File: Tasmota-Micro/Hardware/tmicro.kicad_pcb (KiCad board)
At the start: 4 copper layers, 33.5 x 13 mm, 16 parts, among them P2 CONN_01X02, P3 CONN_01X02, P4 CONN_01X04, P5 CONN_01X02, P6 CONN_01X02, P7 USB_A, Q1 IRLML6244, Q2 IRLML6244, U1 MCP1703, U2 ESP-01v090

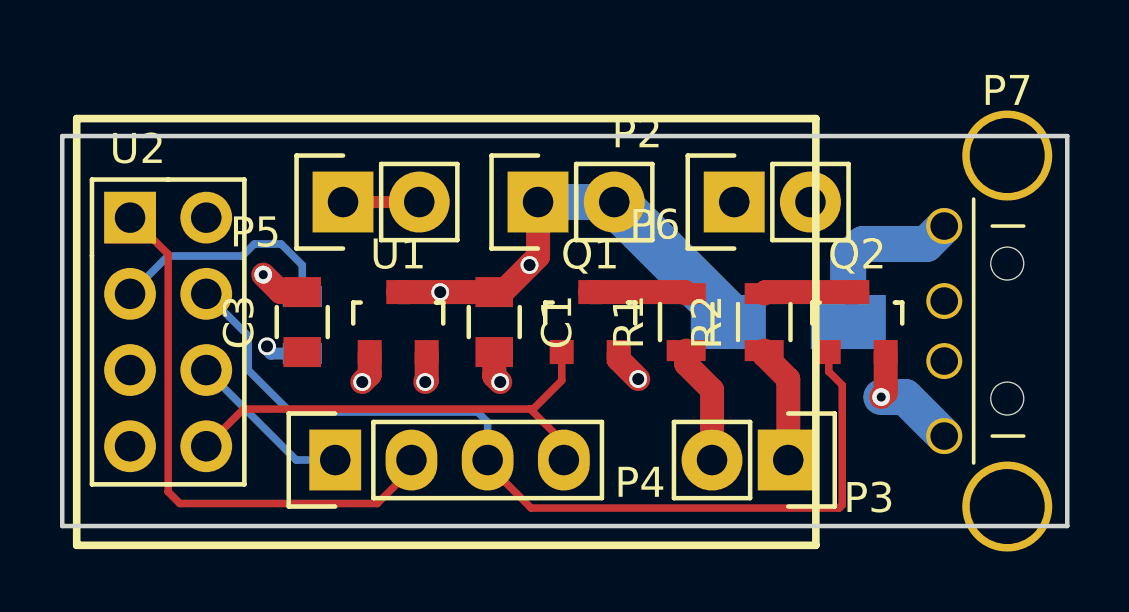
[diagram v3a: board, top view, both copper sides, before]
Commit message: merge back to master as 2 layers
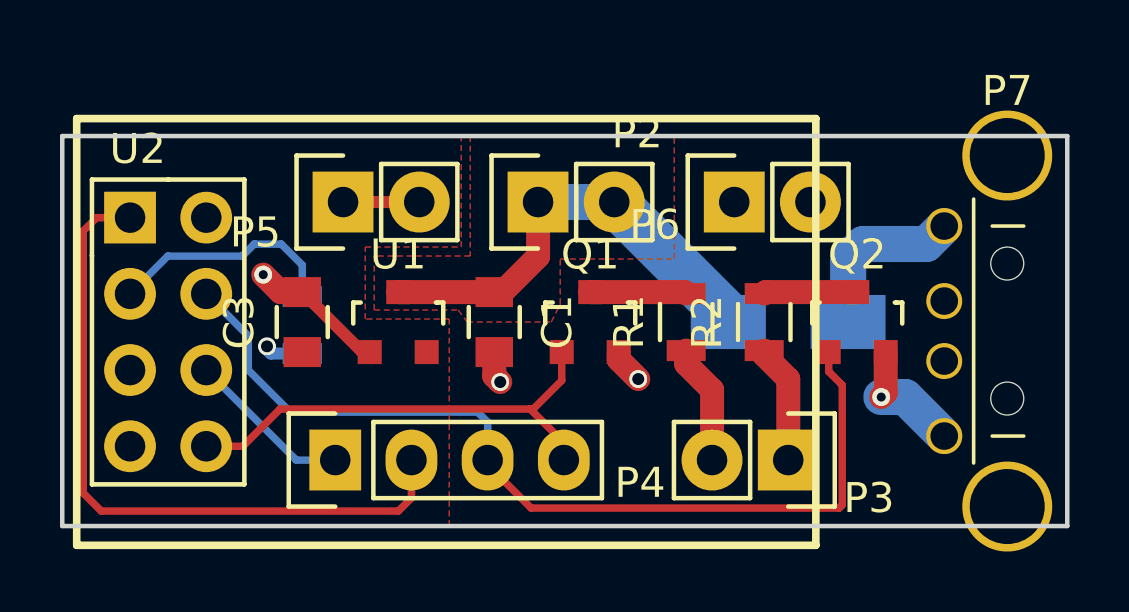
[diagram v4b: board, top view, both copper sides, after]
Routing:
- net TX: track 19.8 -> 23.1 mm
- net GND: track 9.39 -> 11.4 mm, vias 5 -> 4
- net +3V3: track 5.75 -> 4.73 mm, vias 2 -> 1
- net VPP: vias 2 -> 0
- added copper zone on F.Cu, net +3V3
- added copper zone on B.Cu, net GND
- added copper zone on F.Cu, net VPP
- removed copper zone on In1.Cu, net +3V3
- removed copper zone on In2.Cu, net GND
- removed copper zone on In1.Cu, net VPP
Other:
- copper layers 4 -> 2
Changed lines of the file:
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@@
   (general
     (links 31)
-    (no_connects 1)
+    (no_connects 0)
     (area 144.407 102.575 201.425001 126.875)
     (thickness 1.6)
     (drawings 14)
-    (tracks 107)
+    (tracks 97)
     (zones 0)
     (modules 16)
@@
   (layers
     (0 F.Cu signal)
-    (1 In1.Cu signal)
-    (2 In2.Cu signal)
     (31 B.Cu signal)
     (32 B.Adhes user)
@@
     (34 B.Paste user)
     (35 F.Paste user)
-    (36 B.SilkS user)
-    (37 F.SilkS user)
+    (36 B.SilkS user hide)
+    (37 F.SilkS user hide)
     (38 B.Mask user)
     (39 F.Mask user)
@@
   (gr_line (start 184.9 108) (end 151.4 108) (layer Edge.Cuts) (width 0.15))
   (gr_line (start 184.9 121) (end 184.9 108) (layer Edge.Cuts) (width 0.15))
-  (via (at 166.976 112.3) (size 0.6) (drill 0.4) (layers F.Cu B.Cu) (net 1))
-  (via (at 164 113.202) (size 0.6) (drill 0.4) (layers F.Cu B.Cu) (net 1))
-  (segment (start 166.976 112.3) (end 167.26 112.016) (width 0.8) (layer F.Cu) (net 1))
-  (segment (start 166.076 113.2) (end 166.976 112.3) (width 0.8) (layer F.Cu) (net 1) (status 10))
-  (segment (start 164 113.202) (end 165.798 113.202) (width 0.8) (layer F.Cu) (net 1) (status 20))
-  (segment (start 162.6002 113.202) (end 164 113.202) (width 0.8) (layer F.Cu) (net 1) (status 10))
   (segment (start 167.26 110.2) (end 169.8 110.2) (width 1.2) (layer B.Cu) (net 1) (status 30))
   (segment (start 173.601 114.001) (end 169.8 110.2) (width 1.6) (layer B.Cu) (net 1) (status 30))
   (segment (start 173.601 114.2) (end 173.601 114.001) (width 1.2) (layer B.Cu) (net 1) (status 30))
   (segment (start 167.26 112.016) (end 167.26 110.2) (width 0.8) (layer F.Cu) (net 1) (status 20))
+  (segment (start 166.076 113.2) (end 167.26 112.016) (width 0.8) (layer F.Cu) (net 1) (status 10))
   (segment (start 165.8 113.2) (end 166.076 113.2) (width 0.8) (layer F.Cu) (net 1) (status 30))
   (segment (start 162.6 113.202) (end 162.6002 113.202) (width 0.8) (layer F.Cu) (net 1) (status 30))
   (segment (start 165.798 113.202) (end 165.8 113.2) (width 0.8) (layer F.Cu) (net 1) (status 30))
+  (segment (start 162.6002 113.202) (end 165.798 113.202) (width 0.8) (layer F.Cu) (net 1) (status 30))
   (segment (start 162.6002 113.202) (end 162.6 113.2018) (width 0.25) (layer F.Cu) (net 1) (status 30))
-  (segment (start 161.65 115.20076) (end 161.65 115.95) (width 0.8) (layer F.Cu) (net 2) (status 10))
-  (segment (start 161.65 115.95) (end 161.4 116.2) (width 0.8) (layer F.Cu) (net 2))
-  (via (at 161.4 116.2) (size 0.6) (drill 0.4) (layers F.Cu B.Cu) (net 2))
+  (segment (start 161.65 115.20076) (end 161.40076 115.20076) (width 0.4) (layer F.Cu) (net 2) (status 30))
+  (segment (start 161.40076 115.20076) (end 159.4 113.2) (width 0.4) (layer F.Cu) (net 2) (status 30))
   (segment (start 161.65 115.20076) (end 161.60076 115.20076) (width 0.4) (layer F.Cu) (net 2) (status 30))
   (segment (start 169.95 115.20076) (end 169.95 115.45) (width 0.8) (layer F.Cu) (net 2) (status 30))
@@
   (segment (start 178.85 115.201) (end 178.85 115.2008) (width 0.25) (layer F.Cu) (net 2) (status 30))
   (segment (start 169.95 115.201) (end 169.95 115.2008) (width 0.25) (layer F.Cu) (net 2) (status 30))
-  (segment (start 163.55 115.20076) (end 163.55 116.15) (width 0.8) (layer F.Cu) (net 3) (status 10))
-  (segment (start 163.55 116.15) (end 163.5 116.2) (width 0.8) (layer F.Cu) (net 3))
-  (via (at 163.5 116.2) (size 0.6) (drill 0.4) (layers F.Cu B.Cu) (net 3))
   (segment (start 158.22502 115.12502) (end 158.22502 115.010088) (width 0.4) (layer B.Cu) (net 3))
   (segment (start 159.4 115.25) (end 158.35 115.25) (width 0.4) (layer B.Cu) (net 3) (status 10))
@@
   (segment (start 159.2 118.8) (end 156.2 115.8) (width 0.25) (layer B.Cu) (net 6) (status 20))
   (segment (start 160.5 118.8) (end 159.2 118.8) (width 0.25) (layer B.Cu) (net 6) (status 10))
-  (segment (start 153.66 110.72) (end 153.71 110.72) (width 0.25) (layer F.Cu) (net 7))
-  (segment (start 155.32 120.25) (end 161.9 120.25) (width 0.25) (layer F.Cu) (net 7))
-  (segment (start 153.71 110.72) (end 154.93 111.94) (width 0.25) (layer F.Cu) (net 7))
-  (segment (start 154.93 111.94) (end 154.93 119.86) (width 0.25) (layer F.Cu) (net 7))
-  (segment (start 154.93 119.86) (end 155.32 120.25) (width 0.25) (layer F.Cu) (net 7))
-  (segment (start 163.04 119.11) (end 163.04 118.8) (width 0.25) (layer F.Cu) (net 7))
-  (segment (start 161.9 120.25) (end 163.04 119.11) (width 0.25) (layer F.Cu) (net 7))
-  (segment (start 153.66 110.72) (end 153.66 110.86) (width 0.25) (layer F.Cu) (net 7) (status 30))
-  (segment (start 163.04 117.94) (end 163.04 118.8) (width 0.25) (layer F.Cu) (net 7) (status 30))
-  (segment (start 163.04 118.8) (end 162.964602 118.8) (width 0.25) (layer F.Cu) (net 7) (status 30))
+  (segment (start 163.04 120.066) (end 162.606 120.5) (width 0.25) (layer F.Cu) (net 7))
+  (segment (start 163.04 118.8) (end 163.04 120.066) (width 0.25) (layer F.Cu) (net 7) (status 10))
+  (segment (start 162.606 120.5) (end 152.7 120.5) (width 0.25) (layer F.Cu) (net 7))
+  (segment (start 152.7 120.5) (end 152.1 119.9) (width 0.25) (layer F.Cu) (net 7))
+  (segment (start 152.1 119.9) (end 152.1 111.1664) (width 0.25) (layer F.Cu) (net 7))
+  (segment (start 152.1 111.1664) (end 152.5464 110.72) (width 0.25) (layer F.Cu) (net 7))
+  (segment (start 152.5464 110.72) (end 153.66 110.72) (width 0.25) (layer F.Cu) (net 7) (status 20))
   (segment (start 165.58 118.8) (end 165.58 117.534) (width 0.25) (layer B.Cu) (net 8) (status 10))
   (segment (start 165.58 117.534) (end 165.246 117.2) (width 0.25) (layer B.Cu) (net 8))
@@
   (segment (start 177.3 120.4) (end 167.0276 120.4) (width 0.25) (layer F.Cu) (net 8))
   (segment (start 167.0276 120.4) (end 165.58 118.9524) (width 0.25) (layer F.Cu) (net 8) (status 20))
-  (segment (start 167 117.1) (end 157.44 117.1) (width 0.25) (layer F.Cu) (net 9))
-  (segment (start 157.44 117.1) (end 156.2 118.34) (width 0.25) (layer F.Cu) (net 9))
   (segment (start 167 117.1) (end 167.1 117.1) (width 0.25) (layer F.Cu) (net 9))
   (segment (start 167.1 117.1) (end 168.05 116.15) (width 0.25) (layer F.Cu) (net 9))
   (segment (start 168.05 116.15) (end 168.05 115.20076) (width 0.25) (layer F.Cu) (net 9) (status 20))
+  (segment (start 158.661314 117.1) (end 167 117.1) (width 0.25) (layer F.Cu) (net 9))
   (segment (start 167 117.1) (end 168.12 118.22) (width 0.25) (layer F.Cu) (net 9) (status 20))
   (segment (start 168.12 118.22) (end 168.12 118.8) (width 0.25) (layer F.Cu) (net 9) (status 30))
   (segment (start 168.12 118.6476) (end 168.12 118.8) (width 0.25) (layer F.Cu) (net 9) (status 30))
+  (segment (start 156.2 118.34) (end 157.421314 118.34) (width 0.25) (layer F.Cu) (net 9) (status 10))
+  (segment (start 157.421314 118.34) (end 158.661314 117.1) (width 0.25) (layer F.Cu) (net 9))
   (segment (start 168.05 118.73) (end 168.12 118.8) (width 0.25) (layer F.Cu) (net 9) (status 30))
   (segment (start 169 113.202) (end 169.0002 113.202) (width 0.8) (layer F.Cu) (net 10) (status 30))
@@
   (segment (start 177.8998 113.202) (end 177.9 113.2018) (width 0.25) (layer F.Cu) (net 11) (status 30))
   (segment (start 158.7 111.6) (end 159.4 112.3) (width 0.25) (layer B.Cu) (net 12))
-  (segment (start 159.4 112.3) (end 159.4 113.35) (width 0.25) (layer B.Cu) (net 12) (status 20))
+  (segment (start 159.4 112.3) (end 159.4 113.35) (width 0.25) (layer B.Cu) (net 12))
   (segment (start 157.8 111.6) (end 158.7 111.6) (width 0.25) (layer B.Cu) (net 12))
   (segment (start 157.4 112) (end 157.8 111.6) (width 0.25) (layer B.Cu) (net 12))
   (segment (start 154.92 112) (end 157.4 112) (width 0.25) (layer B.Cu) (net 12))
-  (segment (start 153.66 113.26) (end 154.92 112) (width 0.25) (layer B.Cu) (net 12) (status 10))
+  (segment (start 153.66 113.26) (end 154.92 112) (width 0.25) (layer B.Cu) (net 12))
   (segment (start 180.2 111.6) (end 180.8 111) (width 1.2) (layer B.Cu) (net 13) (status 20))
   (segment (start 178.099 111.6) (end 180.2 111.6) (width 1.2) (layer B.Cu) (net 13))
   (segment (start 177.599 112.1) (end 178.099 111.6) (width 1.2) (layer B.Cu) (net 13))
   (segment (start 177.599 114.2) (end 177.599 112.1) (width 1.2) (layer B.Cu) (net 13) (status 10))
-  (zone (net 2) (net_name GND) (layer In2.Cu) (hatch edge 0.508)
+  (zone (net 2) (net_name GND) (layer B.Cu) (hatch edge 0.508)
     (connect_pads yes (clearance 0.25))
     (min_thickness 0.2)
@@
     )
   )
-  (zone (net 1) (net_name VPP) (layer In1.Cu) (hatch edge 0.508)
+  (zone (net 1) (net_name VPP) (layer F.Cu) (hatch edge 0.508)
     (connect_pads yes (clearance 0.25))
     (min_thickness 0.2)
@@
     (polygon
       (pts
-        (xy 165 108) (xy 165 112) (xy 161.7 112) (xy 161.7 113.8) (xy 164.6 113.8)
+        (xy 165 108) (xy 165 112) (xy 161.8 112) (xy 161.8 113.8) (xy 164.6 113.8)
         (xy 164.9 114.2) (xy 167.7 114.2) (xy 168 113.6) (xy 168 112.1) (xy 171.8 112.1)
         (xy 171.8 108)
@@
     )
   )
-  (zone (net 3) (net_name +3V3) (layer In1.Cu) (hatch edge 0.508)
+  (zone (net 3) (net_name +3V3) (layer F.Cu) (hatch edge 0.508)
     (connect_pads yes (clearance 0.25))
     (min_thickness 0.2)
@@
     (polygon
       (pts
-        (xy 151.4 108) (xy 151.4 121) (xy 164.3 121) (xy 164.3 114.1) (xy 161.4 114.1)
-        (xy 161.4 111.7) (xy 164.7 111.7) (xy 164.7 108)
+        (xy 151.4 108) (xy 151.4 121) (xy 164.3 121) (xy 164.3 114.1) (xy 161.5 114.1)
+        (xy 161.5 111.7) (xy 164.7 111.7) (xy 164.7 108)
       )
     )

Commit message: new utasmota with added things (and stuff)
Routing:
- net TX: track 23.1 -> 17.7 mm, vias 0 -> 1
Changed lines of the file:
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@@
     (thickness 1.6)
     (drawings 14)
-    (tracks 97)
+    (tracks 106)
     (zones 0)
     (modules 16)
@@
   (segment (start 159.2 118.8) (end 156.2 115.8) (width 0.25) (layer B.Cu) (net 6) (status 20))
   (segment (start 160.5 118.8) (end 159.2 118.8) (width 0.25) (layer B.Cu) (net 6) (status 10))
-  (segment (start 163.04 120.066) (end 162.606 120.5) (width 0.25) (layer F.Cu) (net 7))
-  (segment (start 163.04 118.8) (end 163.04 120.066) (width 0.25) (layer F.Cu) (net 7) (status 10))
-  (segment (start 162.606 120.5) (end 152.7 120.5) (width 0.25) (layer F.Cu) (net 7))
-  (segment (start 152.7 120.5) (end 152.1 119.9) (width 0.25) (layer F.Cu) (net 7))
-  (segment (start 152.1 119.9) (end 152.1 111.1664) (width 0.25) (layer F.Cu) (net 7))
-  (segment (start 152.1 111.1664) (end 152.5464 110.72) (width 0.25) (layer F.Cu) (net 7))
-  (segment (start 152.5464 110.72) (end 153.66 110.72) (width 0.25) (layer F.Cu) (net 7) (status 20))
+  (segment (start 154.925 113.975) (end 154.925 116.425) (width 0.25) (layer B.Cu) (net 7))
+  (segment (start 154.925 116.425) (end 155.575 117.075) (width 0.25) (layer B.Cu) (net 7))
+  (segment (start 155.575 117.075) (end 156.8 117.075) (width 0.25) (layer B.Cu) (net 7))
+  (segment (start 156.8 117.075) (end 158.925 119.2) (width 0.25) (layer B.Cu) (net 7))
+  (segment (start 158.925 119.2) (end 158.925 120) (width 0.25) (layer B.Cu) (net 7))
+  (segment (start 162.325 120.425) (end 163.04 119.71) (width 0.25) (layer B.Cu) (net 7))
+  (segment (start 163.04 119.71) (end 163.04 118.8) (width 0.25) (layer B.Cu) (net 7))
+  (segment (start 158.925 120) (end 159.35 120.425) (width 0.25) (layer B.Cu) (net 7))
+  (segment (start 159.35 120.425) (end 162.325 120.425) (width 0.25) (layer B.Cu) (net 7))
+  (segment (start 154.925 113.725) (end 154.925 113.975) (width 0.25) (layer F.Cu) (net 7))
+  (via (at 154.925 113.975) (size 0.6) (drill 0.4) (layers F.Cu B.Cu) (net 7))
+  (segment (start 154.925 111.925) (end 154.925 113.725) (width 0.25) (layer F.Cu) (net 7))
+  (segment (start 154.85 111.85) (end 154.925 111.925) (width 0.25) (layer F.Cu) (net 7))
+  (segment (start 154.65 111.65) (end 154.85 111.85) (width 0.25) (layer F.Cu) (net 7))
+  (segment (start 153.72 110.72) (end 154.65 111.65) (width 0.25) (layer F.Cu) (net 7))
+  (segment (start 153.66 110.72) (end 153.72 110.72) (width 0.25) (layer F.Cu) (net 7))
   (segment (start 165.58 118.8) (end 165.58 117.534) (width 0.25) (layer B.Cu) (net 8) (status 10))
   (segment (start 165.58 117.534) (end 165.246 117.2) (width 0.25) (layer B.Cu) (net 8))
@@
   (segment (start 177.8998 113.202) (end 177.9 113.2018) (width 0.25) (layer F.Cu) (net 11) (status 30))
   (segment (start 158.7 111.6) (end 159.4 112.3) (width 0.25) (layer B.Cu) (net 12))
-  (segment (start 159.4 112.3) (end 159.4 113.35) (width 0.25) (layer B.Cu) (net 12))
+  (segment (start 159.4 112.3) (end 159.4 113.35) (width 0.25) (layer B.Cu) (net 12) (status 20))
   (segment (start 157.8 111.6) (end 158.7 111.6) (width 0.25) (layer B.Cu) (net 12))
   (segment (start 157.4 112) (end 157.8 111.6) (width 0.25) (layer B.Cu) (net 12))
   (segment (start 154.92 112) (end 157.4 112) (width 0.25) (layer B.Cu) (net 12))
-  (segment (start 153.66 113.26) (end 154.92 112) (width 0.25) (layer B.Cu) (net 12))
+  (segment (start 153.66 113.26) (end 154.92 112) (width 0.25) (layer B.Cu) (net 12) (status 10))
   (segment (start 180.2 111.6) (end 180.8 111) (width 1.2) (layer B.Cu) (net 13) (status 20))
   (segment (start 178.099 111.6) (end 180.2 111.6) (width 1.2) (layer B.Cu) (net 13))
